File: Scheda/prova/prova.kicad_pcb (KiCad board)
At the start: 2 copper layers, 85 x 40 mm, 28 parts, among them J2 Conn_01x02, J3 Conn_01x02, J4 Signal_Out, J5 Signal_Out, J6 Supply, J7 Test, J8 Test, J9 Vbias, U1 Opamp_Quad

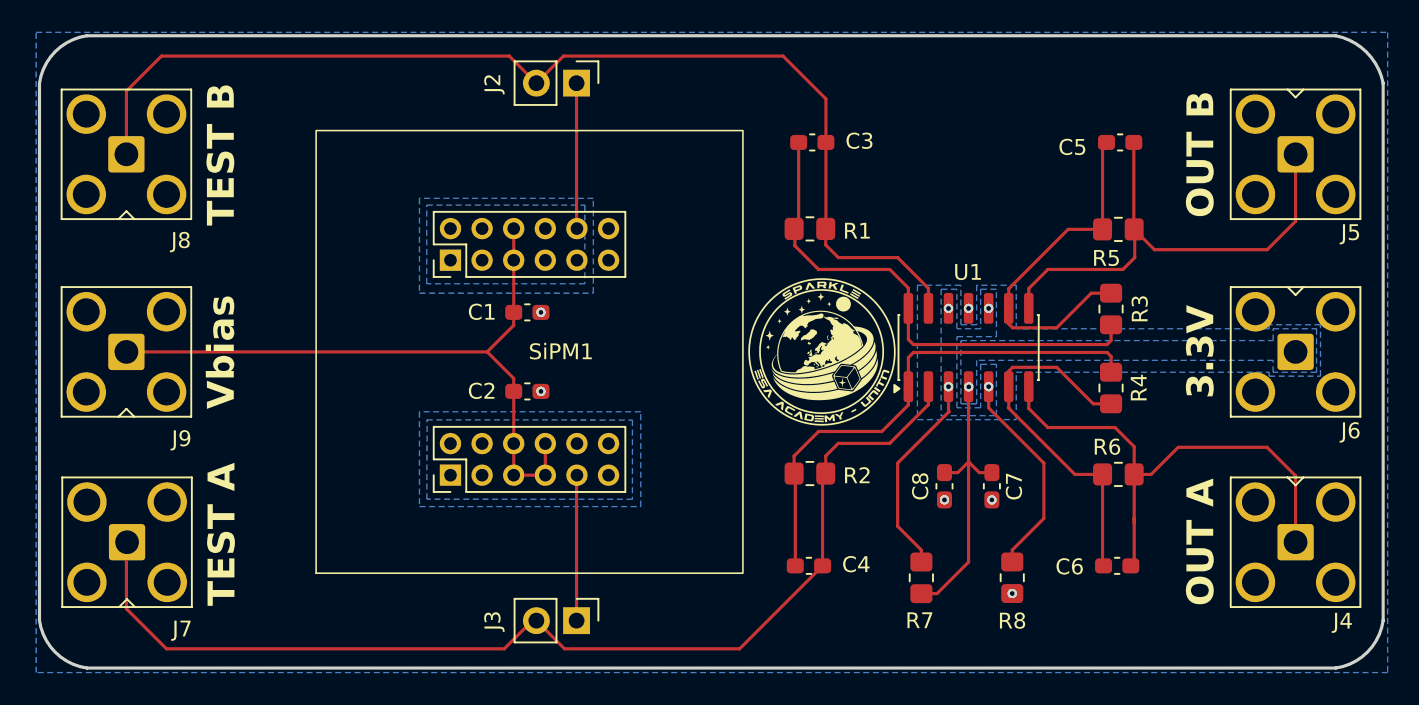
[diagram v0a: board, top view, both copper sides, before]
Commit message: Aggiunta modelli 3D e regolatore
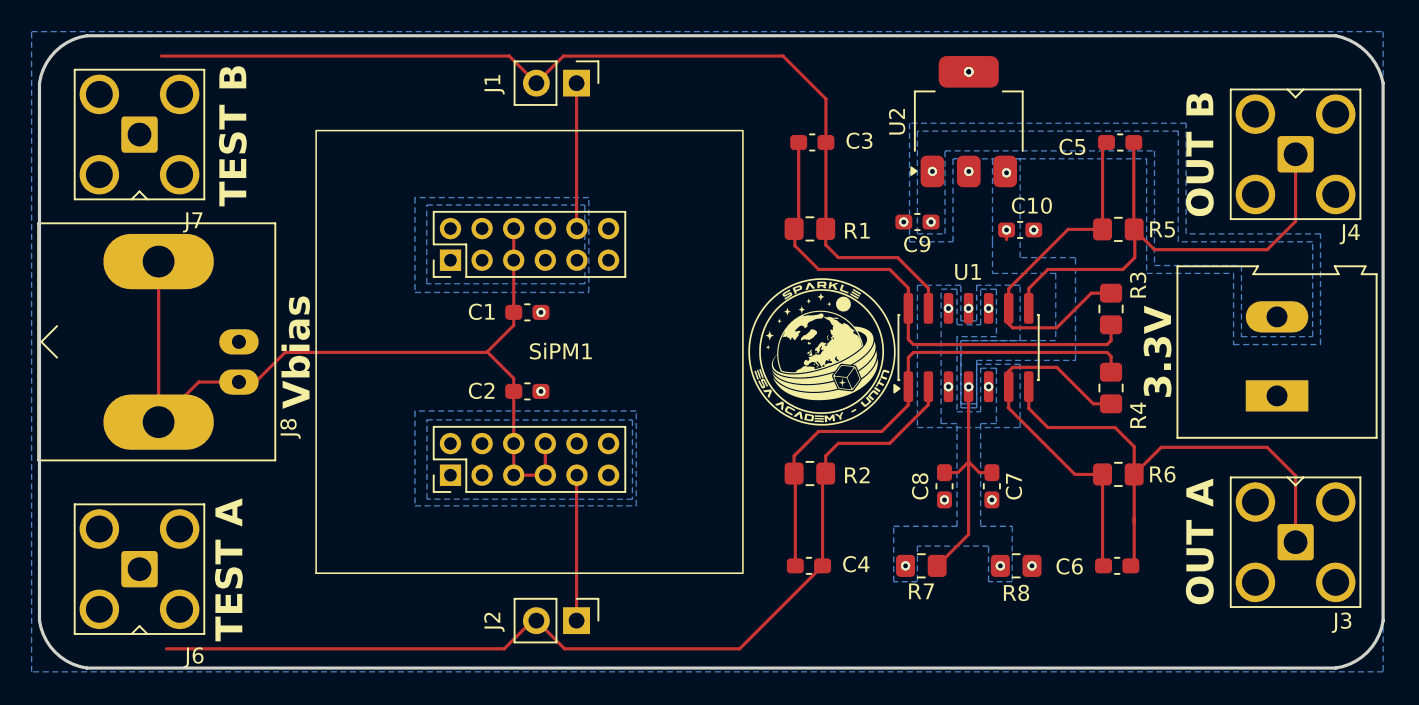
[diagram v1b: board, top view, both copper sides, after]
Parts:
- removed the J6 at (175.9, 103.5)
- removed J9: Vbias, SPaRKLE-Footprints:SMA_Horizontal
- added C10: 4.7u, Capacitor_SMD:C_0603_1608Metric_Pad1.08x0.95mm_HandSolder, F.Cu at (158.5, 95.8)
- added C9: 1u, Capacitor_SMD:C_0603_1608Metric_Pad1.08x0.95mm_HandSolder, F.Cu at (152.0, 95.2)
- added J5: Screw_Terminal_01x02, SPaRKLE-Footprints:TerminalBlock_Altech_AK300-2_P5.00mm, F.Cu at (174.8, 106.2)
- added J8: Conn_Coaxial, Connector_Coaxial:BNC_Amphenol_B6252HB-NPP3G-50_Horizontal, F.Cu at (109.1, 102.8)
- added U2: BD433M2FP3-CE2, Package_TO_SOT_SMD:SOT-223-3_TabPin2, F.Cu at (155.2, 88.9)
- R7, R8: value 1k -> 500
- moved J6 1.88 mm to (102.8, 117.2)
- moved J7 1.50 mm to (102.8, 89.7)
- moved R8 0.79 mm to (158.2, 117.0), turned to 0 degrees
- moved R7 0.76 mm to (152.2, 117.0), turned to 180 degrees
- renumbered J2 to J1, J3 to J2, J4 to J3, J5 to J4, J7 to J6, J8 to J7
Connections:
- R7 pad 1: VREF -> VCC
- R7 pad 2: VCC -> VREF
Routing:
- net VREF: track 26.4 -> 0.00 mm, vias 4 -> 6
- net VBIAS: track 43.8 -> 53.8 mm
- net TEST_A: track 68.9 -> 61.3 mm
- net TEST_B: track 69.9 -> 62.7 mm
- net VCC: track 18.5 -> 16.5 mm, vias 1 -> 3
- net GND: vias 6 -> 12
- net +5V: vias 0 -> 2
- added copper zone on B.Cu, net +5V
